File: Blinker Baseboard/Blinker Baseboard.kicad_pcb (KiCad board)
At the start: 2 copper layers, 53.3 x 76.2 mm, 47 parts, among them J1 L Spinner, J2 R Spinner, J3 L Blinker, J4 R Blinker, J5 Charger - Out, J6 Charger - In, J7 Charger - Bat, Q1 BSS138, Q10 BSS138, Q11 BSS138, Q12 BSS138, Q2 BSS138, Q3 BSS138, Q4 BSS138, Q5 BSS138, Q6 BSS138, Q7 BSS138, Q8 BSS138, Q9 BSS138, SW1 SW_Push, U1 RaspberryPi_Pico

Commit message: r1
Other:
- board text added: "Blinker, base board v1.0 r1 Jim 2024-02-07"
- board text added: "L Blinker"
- board text added: "L Spinner"
- board text added: "R Blinker"
- board text added: "R Spinner"
- board text added: "Raspberry Pi Pico"
- board text removed: "Blinker, base board v1.0 Jim 2024-02-07"

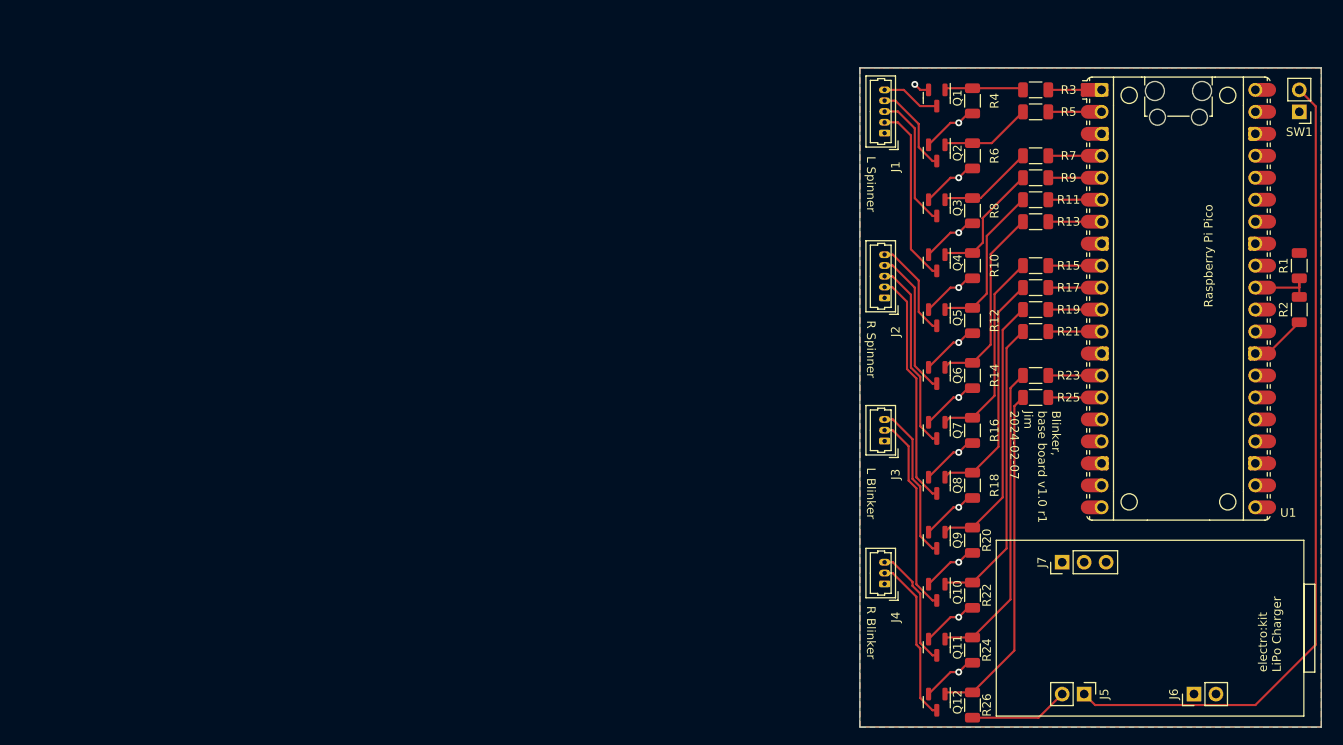
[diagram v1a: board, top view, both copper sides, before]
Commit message: Baseboard rework
R2 became v2.
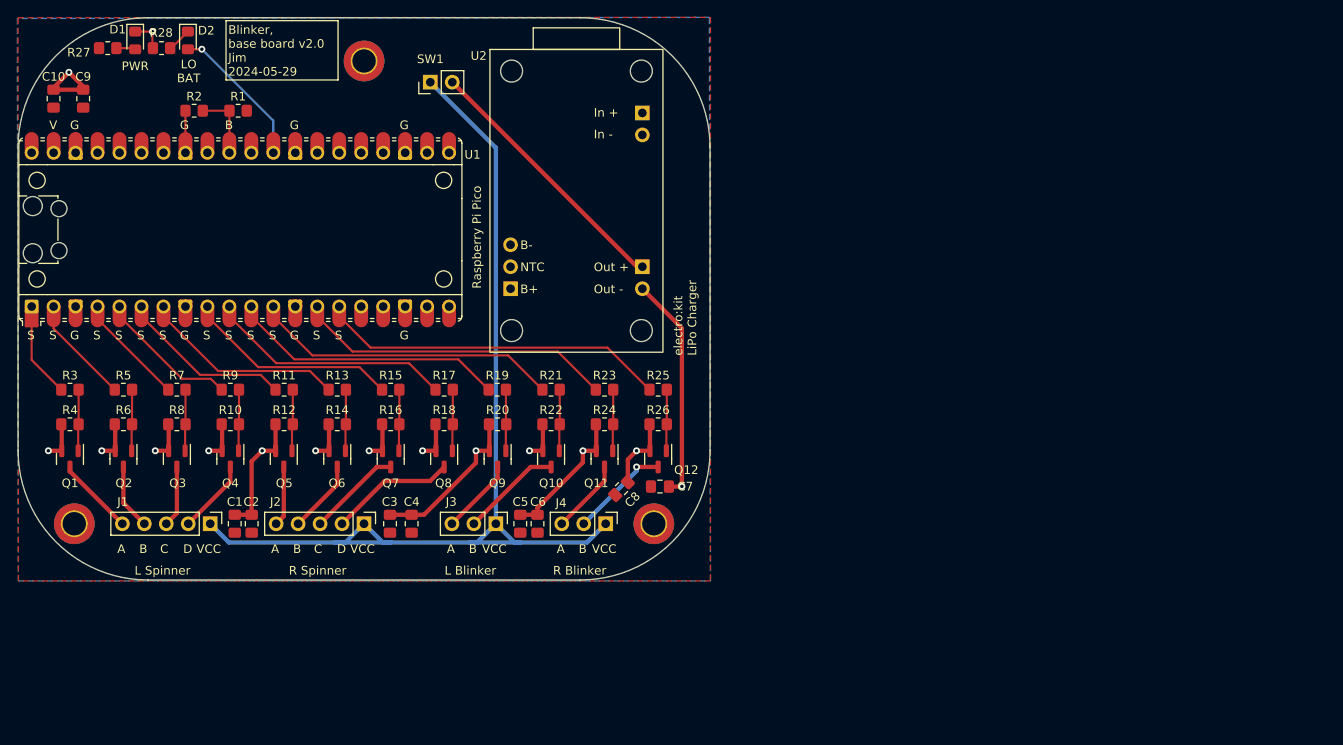
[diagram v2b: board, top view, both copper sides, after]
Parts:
- removed J5: Charger - Out, Connector_PinHeader_2.54mm:PinHeader_1x02_P2.54mm_Vertical
- removed J6: Charger - In, Connector_PinHeader_2.54mm:PinHeader_1x02_P2.54mm_Vertical
- removed J7: Charger - Bat, Connector_PinHeader_2.54mm:PinHeader_1x03_P2.54mm_Vertical
- added C1: C, Capacitor_SMD:C_0805_2012Metric_Pad1.18x1.45mm_HandSolder, F.Cu at (75.0, 103.5)
- added C10: C, Capacitor_SMD:C_0805_2012Metric_Pad1.18x1.45mm_HandSolder, F.Cu at (54.1, 54.4)
- added C2: C, Capacitor_SMD:C_0805_2012Metric_Pad1.18x1.45mm_HandSolder, F.Cu at (77.0, 103.5)
- added C3: C, Capacitor_SMD:C_0805_2012Metric_Pad1.18x1.45mm_HandSolder, F.Cu at (93.0, 103.5)
- added C4: C, Capacitor_SMD:C_0805_2012Metric_Pad1.18x1.45mm_HandSolder, F.Cu at (95.5, 103.5)
- added C5: C, Capacitor_SMD:C_0805_2012Metric_Pad1.18x1.45mm_HandSolder, F.Cu at (108.1, 103.5)
- added C6: C, Capacitor_SMD:C_0805_2012Metric_Pad1.18x1.45mm_HandSolder, F.Cu at (110.0, 103.5)
- added C7: C, Capacitor_SMD:C_0805_2012Metric_Pad1.18x1.45mm_HandSolder, F.Cu at (124.2, 99.2)
- added C8: C, Capacitor_SMD:C_0805_2012Metric_Pad1.18x1.45mm_HandSolder, F.Cu at (119.8, 99.4)
- added C9: C, Capacitor_SMD:C_0805_2012Metric_Pad1.18x1.45mm_HandSolder, F.Cu at (57.5, 54.4)
- added D1: LED, LED_SMD:LED_0805_2012Metric_Pad1.15x1.40mm_HandSolder, F.Cu at (63.5, 47.6)
- added D2: LED, LED_SMD:LED_0805_2012Metric_Pad1.15x1.40mm_HandSolder, F.Cu at (69.6, 47.6)
- added R27: R, Resistor_SMD:R_0805_2012Metric_Pad1.20x1.40mm_HandSolder, F.Cu at (60.4, 48.5)
- added R28: R, Resistor_SMD:R_0805_2012Metric_Pad1.20x1.40mm_HandSolder, F.Cu at (66.6, 48.5)
- added REF**: MountingHole_2.7mm_M2.5_DIN965_Pad_TopBottom, MountingHole:MountingHole_2.7mm_M2.5_DIN965_Pad_TopBottom, F.Cu at (56.5, 103.5)
- added REF**: MountingHole_2.7mm_M2.5_DIN965_Pad_TopBottom, MountingHole:MountingHole_2.7mm_M2.5_DIN965_Pad_TopBottom, F.Cu at (123.5, 103.5)
- added REF**: MountingHole_2.7mm_M2.5_DIN965_Pad_TopBottom, MountingHole:MountingHole_2.7mm_M2.5_DIN965_Pad_TopBottom, F.Cu at (90.0, 50.0)
- added U2: ~, ek:Electrokit LiPo charger, F.Cu at (114.6, 66.2)
- J1, J2: footprint Connector_Molex:Molex_PicoBlade_53047-0510_1x05_P1.25mm_Vertical -> Connector_PinHeader_2.54mm:PinHeader_1x05_P2.54mm_Vertical
- J3, J4: footprint Connector_Molex:Molex_PicoBlade_53047-0310_1x03_P1.25mm_Vertical -> Connector_PinHeader_2.54mm:PinHeader_1x03_P2.54mm_Vertical
- R1, R10, R11, R12, R13, R14, R15, R16, R17, R18, R19, R2, R20, R21, R22, R23, R24, R25, R26, R3, R4, R5, R6, R7, R8, R9: footprint Resistor_SMD:R_1206_3216Metric -> Resistor_SMD:R_0805_2012Metric_Pad1.20x1.40mm_HandSolder
- moved R2 129.8 mm to (70.4, 55.8), turned to 0 degrees
- moved R1 124.0 mm to (75.4, 55.8), turned to 0 degrees
- moved R3 116.9 mm to (56.0, 88.0), turned to 180 degrees
- moved R4 110.8 mm to (56.0, 92.0), turned to 0 degrees
- moved R5 110.2 mm to (62.2, 88.0), turned to 180 degrees
- moved U1 108.7 mm to (75.7, 69.5), turned to 90 degrees
- moved Q1 108.5 mm to (56.0, 96.0)
- moved R6 103.0 mm to (62.2, 92.0), turned to 0 degrees
- moved R7 102.9 mm to (68.4, 88.0), turned to 180 degrees
- moved SW1 100.5 mm to (97.7, 52.5), turned to 90 degrees
- moved Q2 100.5 mm to (62.2, 96.0)
- moved R9 96.3 mm to (74.5, 88.0), turned to 180 degrees
- moved R8 95.2 mm to (68.4, 92.0), turned to 0 degrees
- moved Q3 92.5 mm to (68.4, 96.0)
- moved J1 90.1 mm to (72.2, 103.5), turned to -90 degrees
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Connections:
- U1 pad 29: unconnected-(U1-GPIO22-Pad29) -> Net-(D2-A)
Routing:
- net VCC: track 0.00 -> 117.6 mm
- net Net-(U2-Out_+): track 95.1 -> 30.8 mm
- net GND: track 92.8 -> 139.1 mm, vias 12 -> 15
- net Net-(U1-GPIO11): track 6.16 -> 40.5 mm
- net Net-(Q12-G): track 39.8 -> 7.08 mm
- net Net-(U1-GPIO10): track 6.16 -> 36.9 mm
- net Net-(U1-GPIO9): track 6.16 -> 35.8 mm
- net Net-(Q11-G): track 36.0 -> 7.08 mm
- net Net-(Q10-G): track 34.7 -> 7.08 mm
- net Net-(U1-GPIO8): track 6.16 -> 32.1 mm
- net Net-(Q9-G): track 31.0 -> 7.10 mm
- net Net-(U1-GPIO7): track 6.16 -> 28.5 mm
- net Net-(Q8-G): track 27.2 -> 7.08 mm
- net Net-(U1-GPIO6): track 6.16 -> 24.8 mm
- net Net-(U1-GPIO5): track 6.16 -> 23.7 mm
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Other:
- board size 53.3 x 76.2 mm -> 80 x 65 mm
- board text added: "A"
- board text added: "B"
- board text added: "Blinker, base board v2.0 Jim 2024-05-29"
- board text added: "C"
- board text added: "D"
- board text added: "D1, D2: LED 0805 (red) C1, C3, C5, C7, C9: Capacitor 0805 100 nF C2, C4, C6, C8, C10: Capacitor 0805 10 uF R1, R2: Resistor 0805 10 kohm R3, R5, R7, R9, R11, R13, R15, R17, R19, R21, R23, R25: Resistor 0805 0-50 ohm R4, R6, R8, R10, R12, R14, R16, R18, R20, R22, R24, R26: Resistor 0805 10 - 47 kohm R27, R28: Resistor 0805 1 kohm Q1 - Q12: MOSFET SOT-23 FDV303N or BSS138 U1: Raspberry Pi Pico"
- board text added: "G"
- board text added: "LO BAT"
- board text added: "PWR"
- board text added: "Raspberry Pi Pico Markings: V - VIN G - GND B - Battery guage S - Signal"
- board text added: "S"
- board text added: "V"
- board text added: "VCC"
- board text removed: "Blinker, base board v1.0 r1 Jim 2024-02-07"
